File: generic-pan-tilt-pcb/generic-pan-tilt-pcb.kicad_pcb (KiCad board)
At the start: 2 copper layers, 104 x 57 mm, 85 parts, among them J1 B4P-VH-FB-B, J10 USB4105-GF-A, J11 Conn_01x08, J12 Conn_01x08, J13 Conn_01x05, J2 NC5MAV, J3 NC5FAV, J5 BM03B-SRSS-TBT, J7 BM03B-SRSS-TBT, J8 B12B-PH-SM4-TBT, J9 B12B-PH-SM4-TBT, SW1 PTS 647 SK70 SMTR2 LFS, SW2 PTS 647 SK70 SMTR2 LFS, SW3 219-12LPST, U1 RP2040, U2 W25Q128JVS, U3 AP63203WU, U4 ISO1450DW, U5 MCP23017_SO, U6 LIS3DH, Y1 ABM8-272-T3

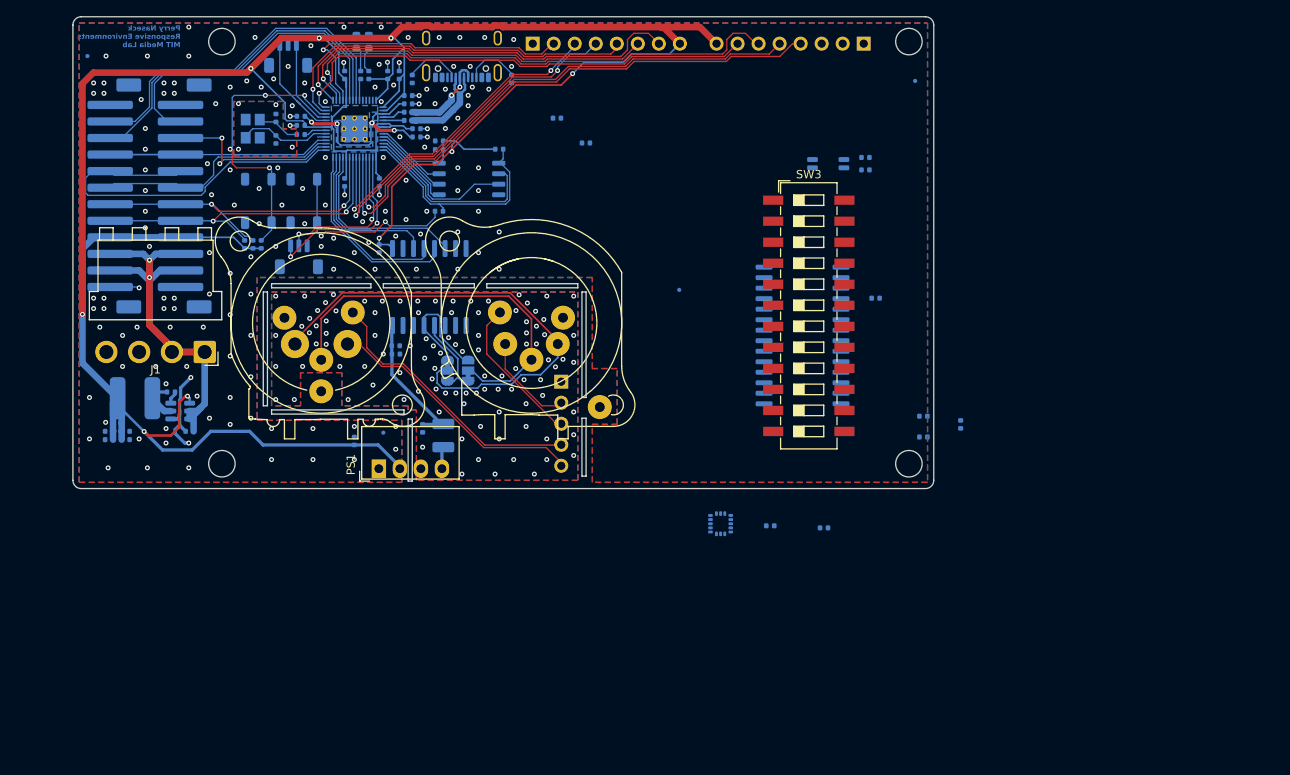
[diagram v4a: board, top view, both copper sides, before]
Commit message: add more fiducials
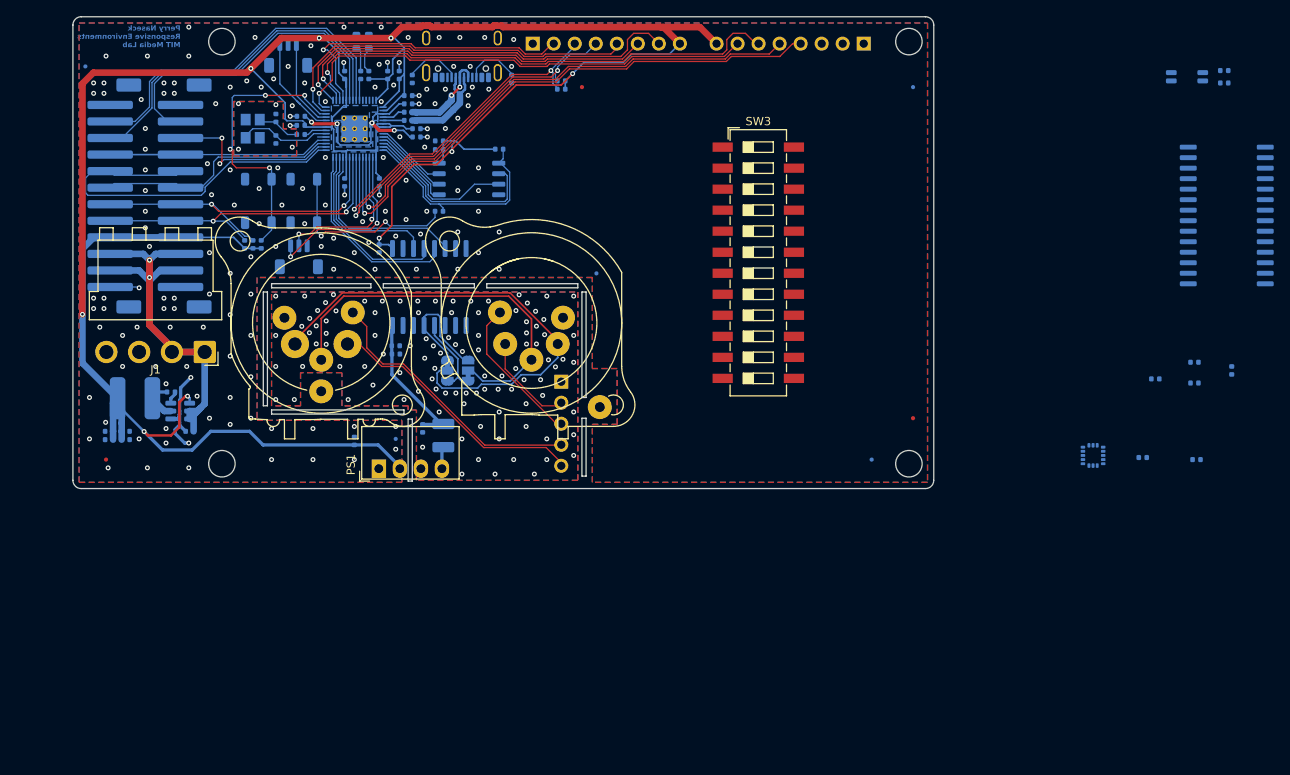
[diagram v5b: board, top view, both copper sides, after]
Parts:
- added FID5: Fiducial, Fiducial:Fiducial_0.5mm_Mask1mm, B.Cu at (177.5, 120.0)
- added FID6: Fiducial, Fiducial:Fiducial_0.5mm_Mask1mm, F.Cu at (85.0, 120.0)
- added FID7: Fiducial, Fiducial:Fiducial_0.5mm_Mask1mm, F.Cu at (182.5, 115.0)
- added FID8: Fiducial, Fiducial:Fiducial_0.5mm_Mask1mm, F.Cu at (142.5, 75.0)
- moved U5 53.3 mm to (220.4, 90.5)
- moved C29 45.8 mm to (210.2, 119.8)
- moved C30 45.8 mm to (216.8, 120.0)
- moved U6 45.8 mm to (204.2, 119.5)
- moved D3 44.6 mm to (215.6, 73.8)
- moved R18 44.6 mm to (220.1, 74.5)
- moved R19 44.6 mm to (220.1, 73.0)
- moved R15 35.2 mm to (211.8, 110.2)
- moved R16 33.4 mm to (216.5, 108.2)
- moved C28 33.4 mm to (221.0, 109.2)
- moved R17 33.4 mm to (216.5, 110.8)
- moved FID4 10.2 mm to (144.2, 97.5)
- moved SW3 8.85 mm to (163.8, 96.2)
- moved R12 7.15 mm to (140.0, 75.2), turned to 0 degrees
- moved R11 4.53 mm to (140.0, 74.2), turned to 0 degrees
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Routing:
- net /I2C0_SCL: track 41.5 -> 44.1 mm
- net +3V3: track 360.0 -> 362.2 mm
- net /I2C0_SDA: track 46.1 -> 47.8 mm

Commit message: routing done, add oshw and license
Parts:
- added SYM1: Logo_Open_Hardware_Small, Symbol:OSHW-Logo2_7.3x6mm_SilkScreen, B.Cu at (107.5, 119.8)
- moved C30 93.1 mm to (133.2, 78.8)
- moved C29 87.7 mm to (133.2, 77.8)
- moved U6 79.8 mm to (136.2, 77.7), turned to -90 degrees
- moved R17 50.6 mm to (168.0, 96.2), turned to 0 degrees
- moved R16 50.3 mm to (168.0, 94.9), turned to 0 degrees
- moved R15 45.6 mm to (168.0, 97.4), turned to 0 degrees
- moved U5 45.3 mm to (175.2, 92.9), turned to 180 degrees
- moved R19 43.7 mm to (177.2, 81.5)
- moved R18 43.6 mm to (177.2, 82.5)
- moved D3 43.4 mm to (173.0, 82.0)
- moved C28 42.3 mm to (181.8, 93.5), turned to 90 degrees
- moved SW3 10.2 mm to (173.0, 100.5), turned to 180 degrees
- moved FID6 7.50 mm to (92.5, 120.0)
- moved FID2 2.50 mm to (180.0, 75.0)
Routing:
- net +3V3: track 362.2 -> 457.3 mm, vias 9 -> 13
- net /I2C0_SDA: track 47.8 -> 129.4 mm, vias 2 -> 3
- net /I2C0_SCL: track 44.1 -> 122.6 mm
- net /generic-pan-tilt-pcb_hid/DIP0: track 0.00 -> 29.6 mm, vias 0 -> 1
- net /generic-pan-tilt-pcb_hid/DIP1: track 0.00 -> 25.6 mm, vias 0 -> 1
- net /generic-pan-tilt-pcb_hid/DIP2: track 0.00 -> 21.6 mm, vias 0 -> 1
- net /generic-pan-tilt-pcb_hid/DIP3: track 0.00 -> 17.8 mm, vias 0 -> 1
- net /generic-pan-tilt-pcb_hid/DIP4: track 0.00 -> 15.2 mm, vias 0 -> 1
- net /generic-pan-tilt-pcb_hid/DIP5: track 0.00 -> 14.5 mm, vias 0 -> 1
- net /generic-pan-tilt-pcb_hid/DIP6: track 0.00 -> 12.7 mm, vias 0 -> 1
- net /generic-pan-tilt-pcb_hid/DIP7: track 0.00 -> 11.1 mm, vias 0 -> 1
- net /generic-pan-tilt-pcb_hid/DIP8: track 0.00 -> 10.1 mm, vias 0 -> 1
- net /generic-pan-tilt-pcb_hid/DIP9: track 0.00 -> 9.08 mm, vias 0 -> 1
- net /generic-pan-tilt-pcb_hid/LED1_G: track 0.00 -> 8.39 mm
- net /generic-pan-tilt-pcb_hid/DIP10: track 0.00 -> 6.27 mm, vias 0 -> 1
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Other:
- board text added: "Licensed under CERN-OHL-P v2"
- board text added: "https://github.com/mitmedialab/generic-pan-tilt-pcb/"

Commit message: dippity dip dip dip chip
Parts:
- SW3: footprint Button_Switch_SMD:SW_DIP_SPSTx12_Slide_6.7x32.04mm_W8.61mm_P2.54mm_LowProfile -> Button_Switch_THT:SW_DIP_SPSTx12_Slide_9.78x32.66mm_W7.62mm_P2.54mm
- moved FID7 40.0 mm to (182.5, 75.0)
- moved C28 21.2 mm to (175.2, 73.3), turned to 180 degrees
- moved SW3 17.1 mm to (176.8, 117.2)
- moved R15 15.3 mm to (179.2, 87.0), turned to 90 degrees
- moved R19 14.1 mm to (163.5, 84.8), turned to 90 degrees
- moved R17 13.5 mm to (177.9, 87.0), turned to 90 degrees
- moved U5 13.0 mm to (174.7, 79.9), turned to -90 degrees
- moved R18 12.9 mm to (164.5, 84.8), turned to -90 degrees
- moved FID2 12.7 mm to (182.5, 87.5)
- moved R16 11.7 mm to (176.7, 87.0), turned to 90 degrees
- moved D3 10.3 mm to (166.0, 89.5), turned to -90 degrees
- moved FID8 2.50 mm to (145.0, 75.0)
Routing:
- net +3V3: track 457.3 -> 424.0 mm, vias 13 -> 14
- net /I2C0_SDA: track 129.4 -> 101.1 mm
- net /I2C0_SCL: track 122.6 -> 94.6 mm
- net /generic-pan-tilt-pcb_hid/DIP3: track 17.8 -> 35.5 mm, vias 1 -> 0
- net /generic-pan-tilt-pcb_hid/DIP2: track 21.6 -> 38.8 mm, vias 1 -> 0
- net /generic-pan-tilt-pcb_hid/DIP1: track 25.6 -> 41.6 mm, vias 1 -> 0
- net /generic-pan-tilt-pcb_hid/DIP0: track 29.6 -> 44.9 mm, vias 1 -> 0
- net /generic-pan-tilt-pcb_hid/DIP4: track 15.2 -> 30.4 mm
- net /generic-pan-tilt-pcb_hid/DIP5: track 14.5 -> 28.6 mm
- net /generic-pan-tilt-pcb_hid/DIP6: track 12.7 -> 26.8 mm
- net /generic-pan-tilt-pcb_hid/DIP7: track 11.1 -> 25.0 mm
- net /generic-pan-tilt-pcb_hid/DIP10: track 6.27 -> 19.5 mm
- net /generic-pan-tilt-pcb_hid/DIP8: track 10.1 -> 23.2 mm
- net /generic-pan-tilt-pcb_hid/DIP9: track 9.08 -> 21.3 mm
- net /generic-pan-tilt-pcb_hid/DIP11: track 5.76 -> 16.8 mm
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
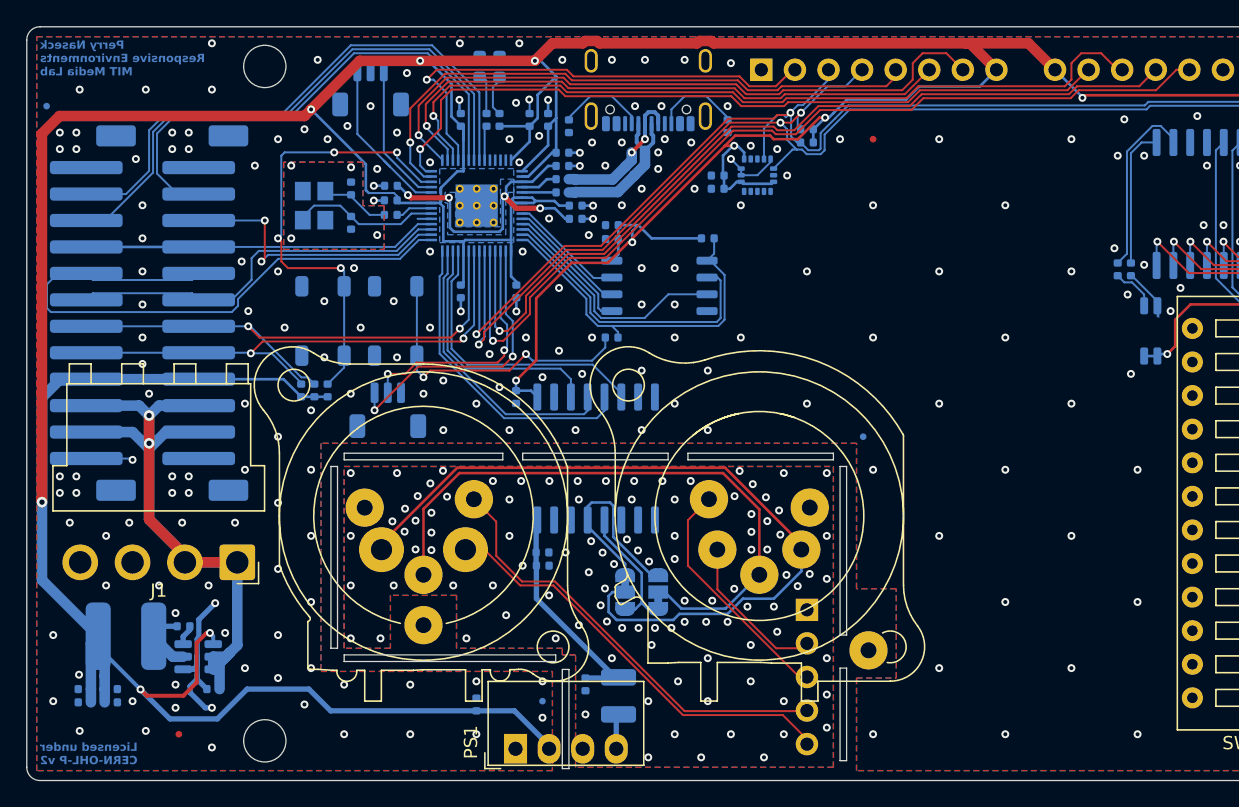
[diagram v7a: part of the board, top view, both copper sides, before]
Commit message: fix all drc and erc
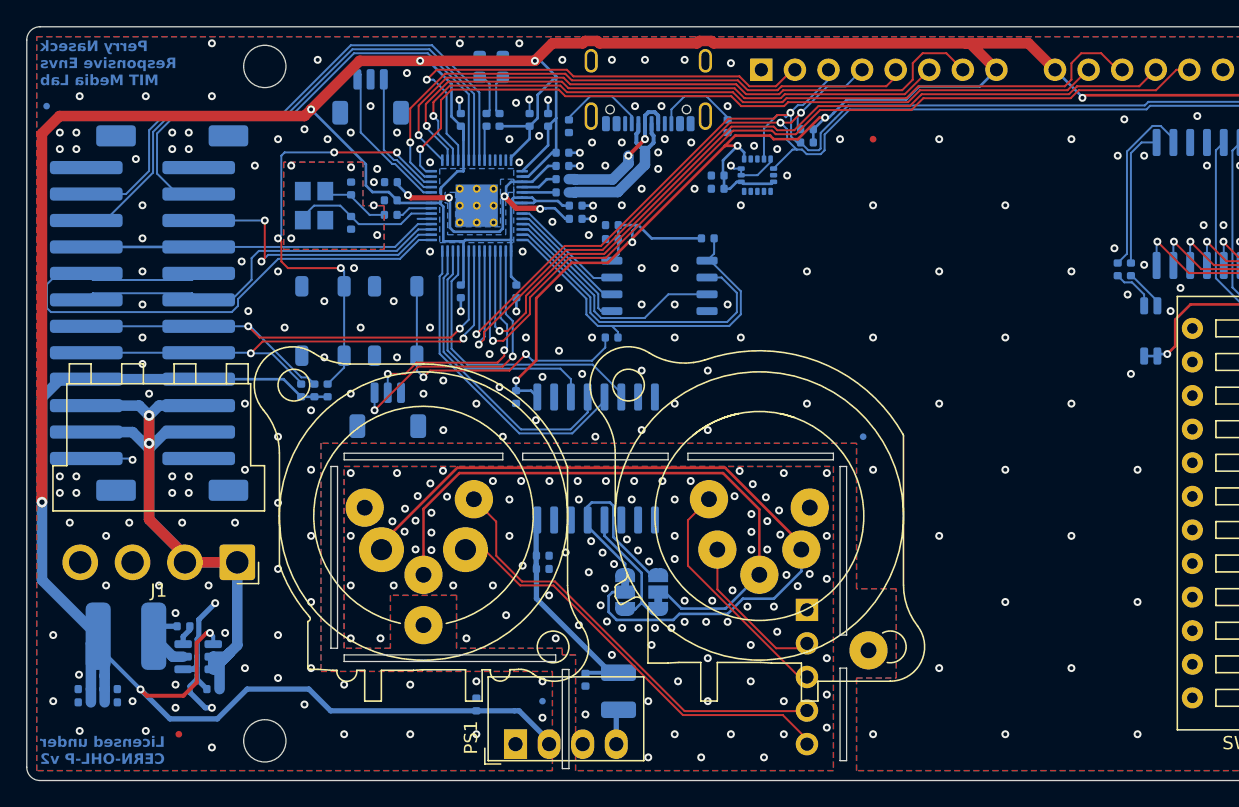
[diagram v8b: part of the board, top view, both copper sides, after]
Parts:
- U1: footprint Package_DFN_QFN:QFN-56-1EP_7x7mm_P0.4mm_EP3.2x3.2mm -> generic-pan-tilt-pcb:RP2040_QFN-56-1EP_7x7mm_P0.4mm_EP3.2x3.2mm
- moved J5 0.62 mm to (107.0, 71.8)
- moved C26 0.35 mm to (123.2, 115.9)
- moved L2 0.35 mm to (125.8, 116.8)
- moved PS1 0.35 mm to (118.0, 120.8)
- moved C5 0.28 mm to (108.5, 78.2)
- moved C25 0.25 mm to (120.0, 106.5)
- moved C27 0.25 mm to (120.0, 107.5)
- moved D1 0.25 mm to (117.0, 69.5)
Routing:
- net GND: track 31.8 -> 30.0 mm, vias 235 -> 237
- net /generic-pan-tilt-pcb_rp2040/QSPI_SD1: track 22.5 -> 24.2 mm
- net /BOOTSEL: track 27.3 -> 28.8 mm
- net /RS485_~{RE}: track 21.7 -> 22.8 mm
- net Net-(D3-K1): track 4.24 -> 3.24 mm
- net /SWCLK: track 12.8 -> 12.0 mm
- net +3V3: track 424.0 -> 423.3 mm
- net /RS485_DE: track 23.6 -> 24.1 mm
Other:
- board text added: "Perry Naseck Responsive Envs MIT Media Lab"
- board text removed: "Perry Naseck Responsive Environments MIT Media Lab"
